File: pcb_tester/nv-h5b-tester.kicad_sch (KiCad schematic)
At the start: 17 parts, among them J1 PSH02-03, J2 Conn_01x01, J3 Conn_01x01, J4 Conn_01x01, J5 Conn_01x01, J6 Conn_01x01, J7 Conn_01x01, U1 ATtiny25-20SS

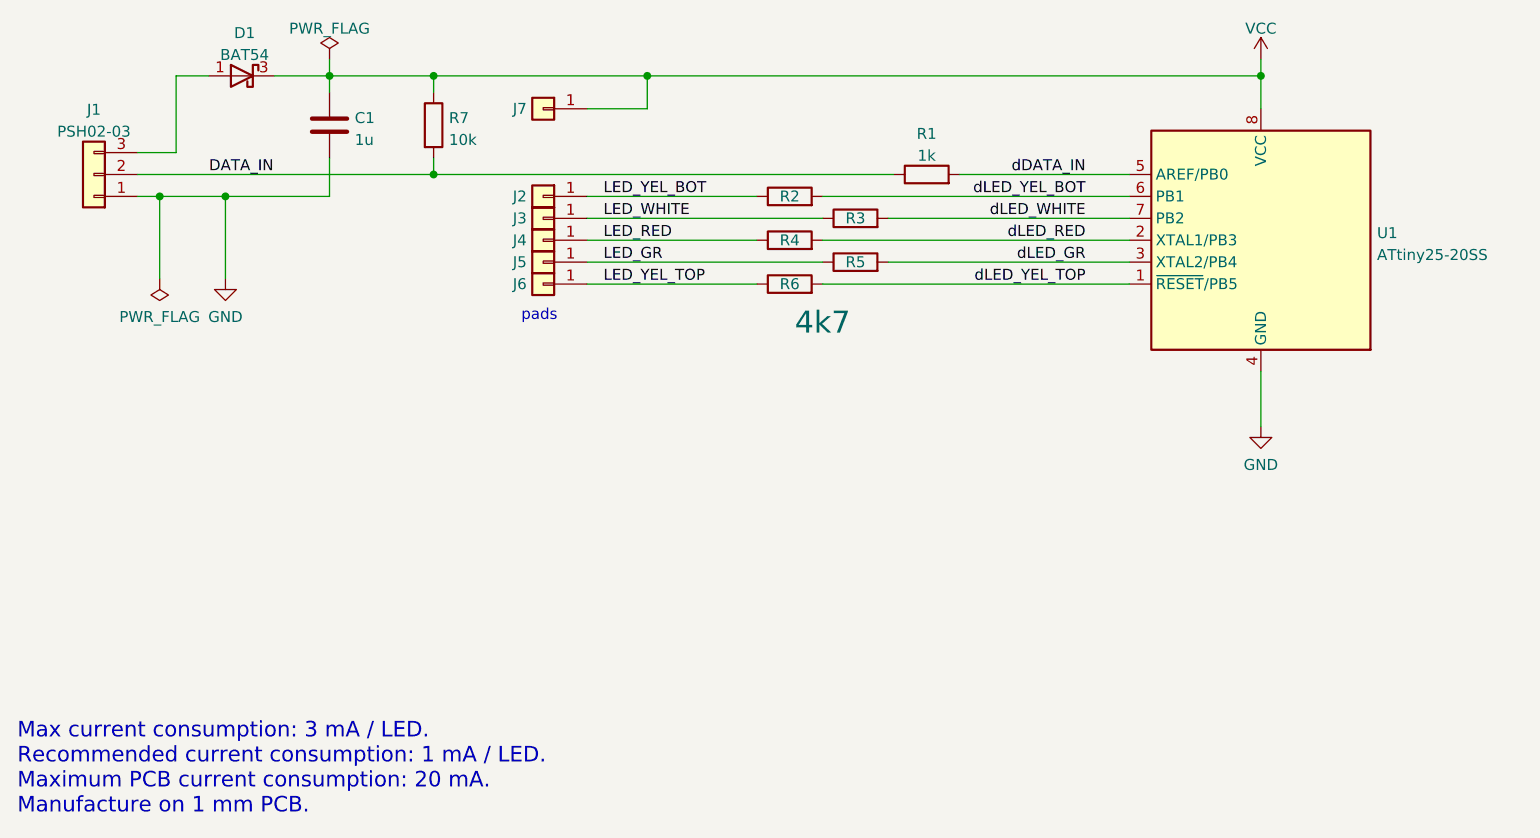
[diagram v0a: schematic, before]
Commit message: Tester: add LEDs to chematics, route PCB.
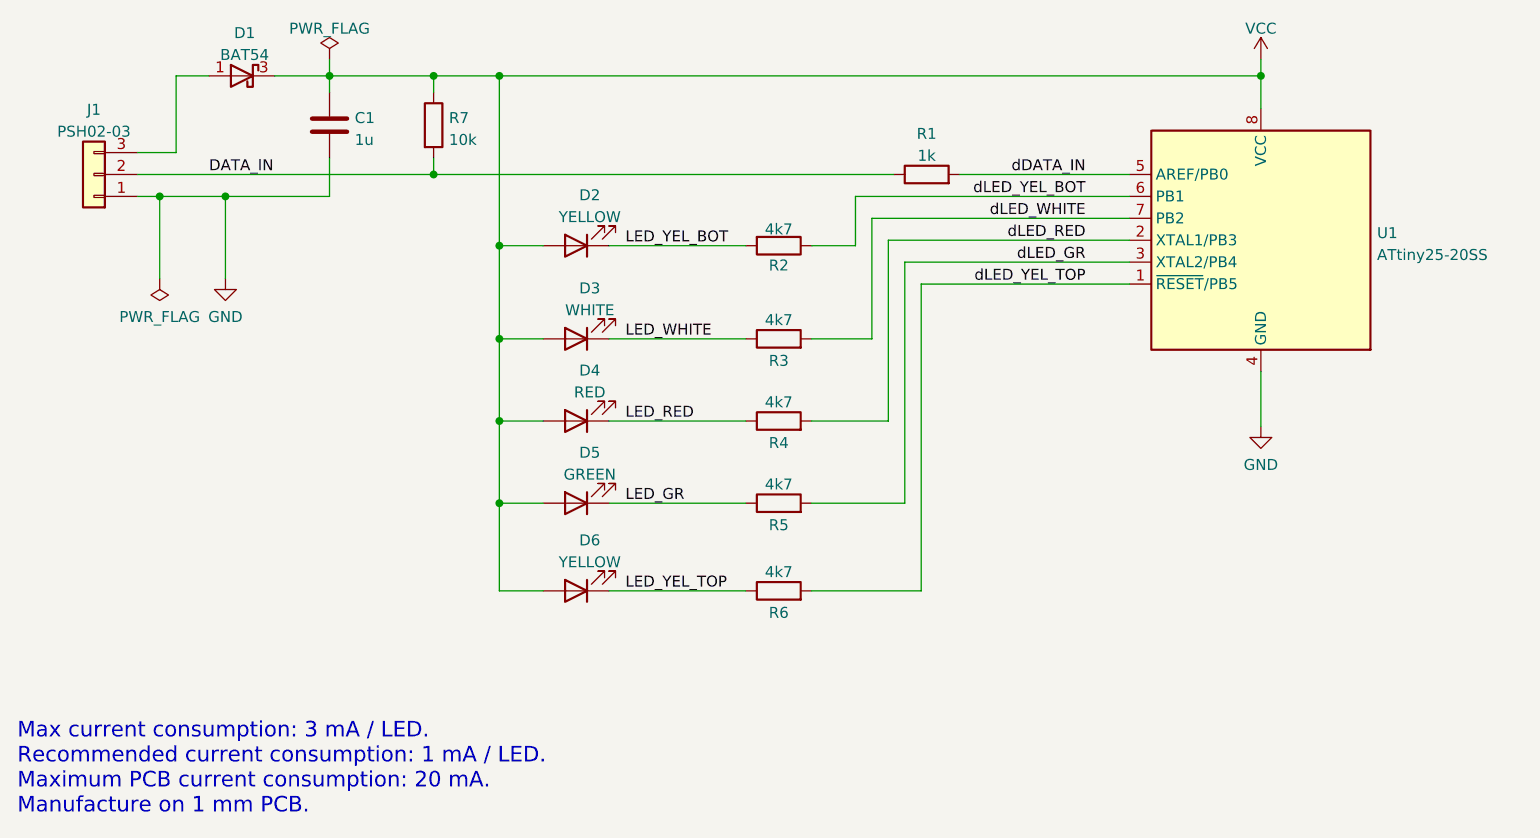
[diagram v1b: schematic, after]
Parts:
- removed J2, J3, J4, J5, J6, J7: Conn_01x01, TestPoint:TestPoint_Keystone_5015_Micro-Minature, symbol Connector_Generic:Conn_01x01
- added D2, D6: YELLOW, LED_SMD:LED_0805_2012Metric, symbol Device:LED
- added D3: WHITE, LED_SMD:LED_0805_2012Metric, symbol Device:LED
- added D4: RED, LED_SMD:LED_0805_2012Metric, symbol Device:LED
- added D5: GREEN, LED_SMD:LED_0805_2012Metric, symbol Device:LED
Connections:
- net LED_GR: now also D5.1 (K)
- net LED_RED: now also D4.1 (K)
- net LED_WHITE: now also D3.1 (K)
- net LED_YEL_BOT: now also R2.2, D2.1 (K); no longer R2.1
- net LED_YEL_TOP: now also D6.1 (K)
- net VCC: now also D2.2 (A), D3.2 (A), D4.2 (A), D5.2 (A), D6.2 (A)
- net dLED_YEL_BOT: now also R2.1; no longer R2.2
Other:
- note removed: "pads"
- company: S-COM decoder -> S-COM decoder with LEDs
- title: NV-H5B -> NV-H5B test signal
- moved on the sheet: R2, R3, R4, R5, R6
